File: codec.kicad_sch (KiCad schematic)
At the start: 24 parts, among them U1 UDA1380HN_N2

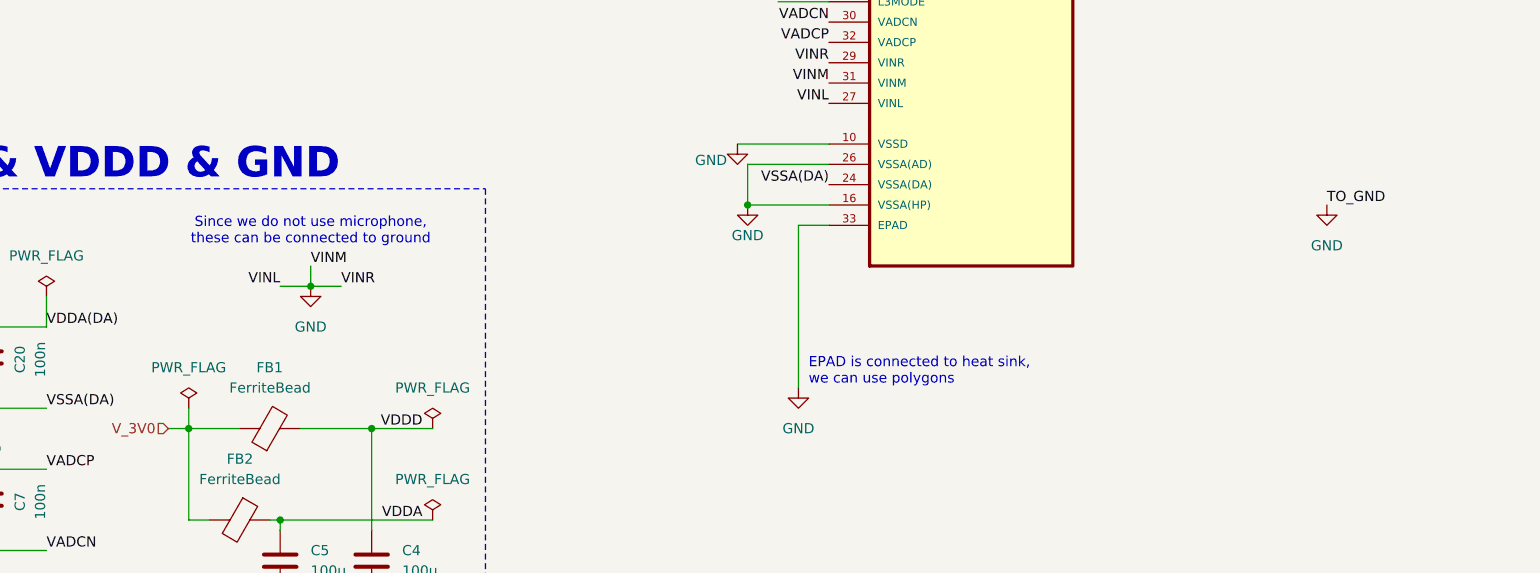
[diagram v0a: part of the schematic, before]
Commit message: Added voltage source for testing to main
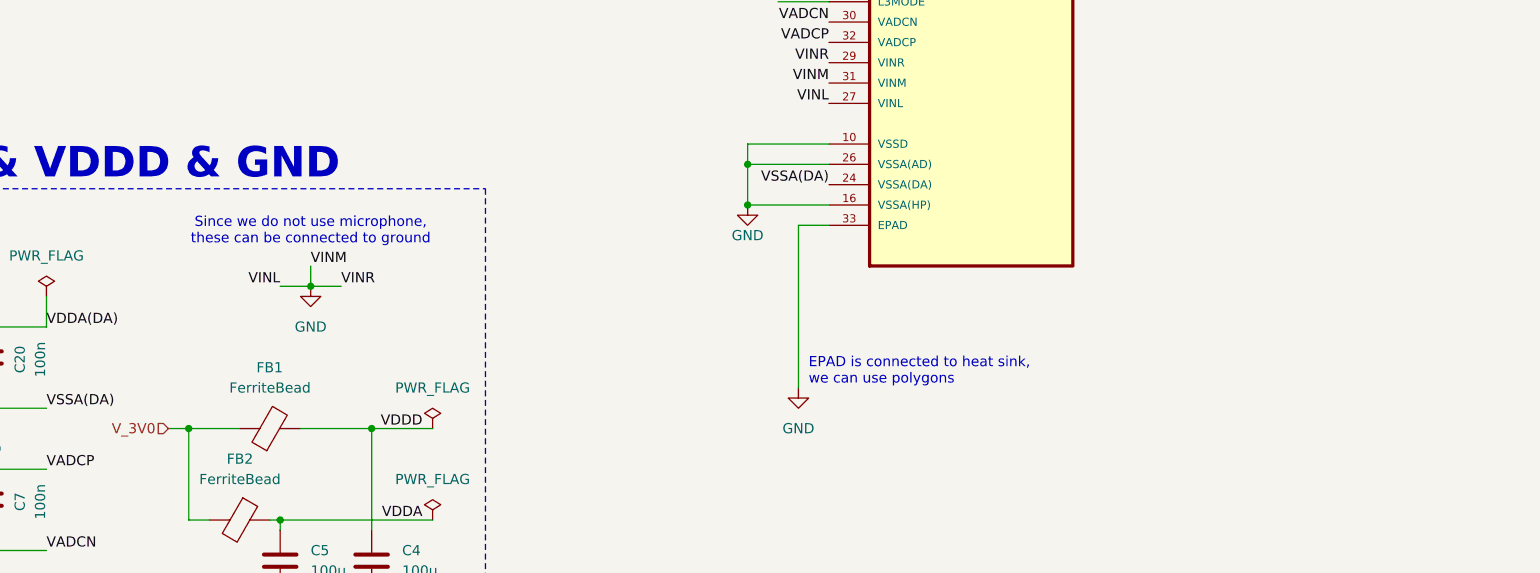
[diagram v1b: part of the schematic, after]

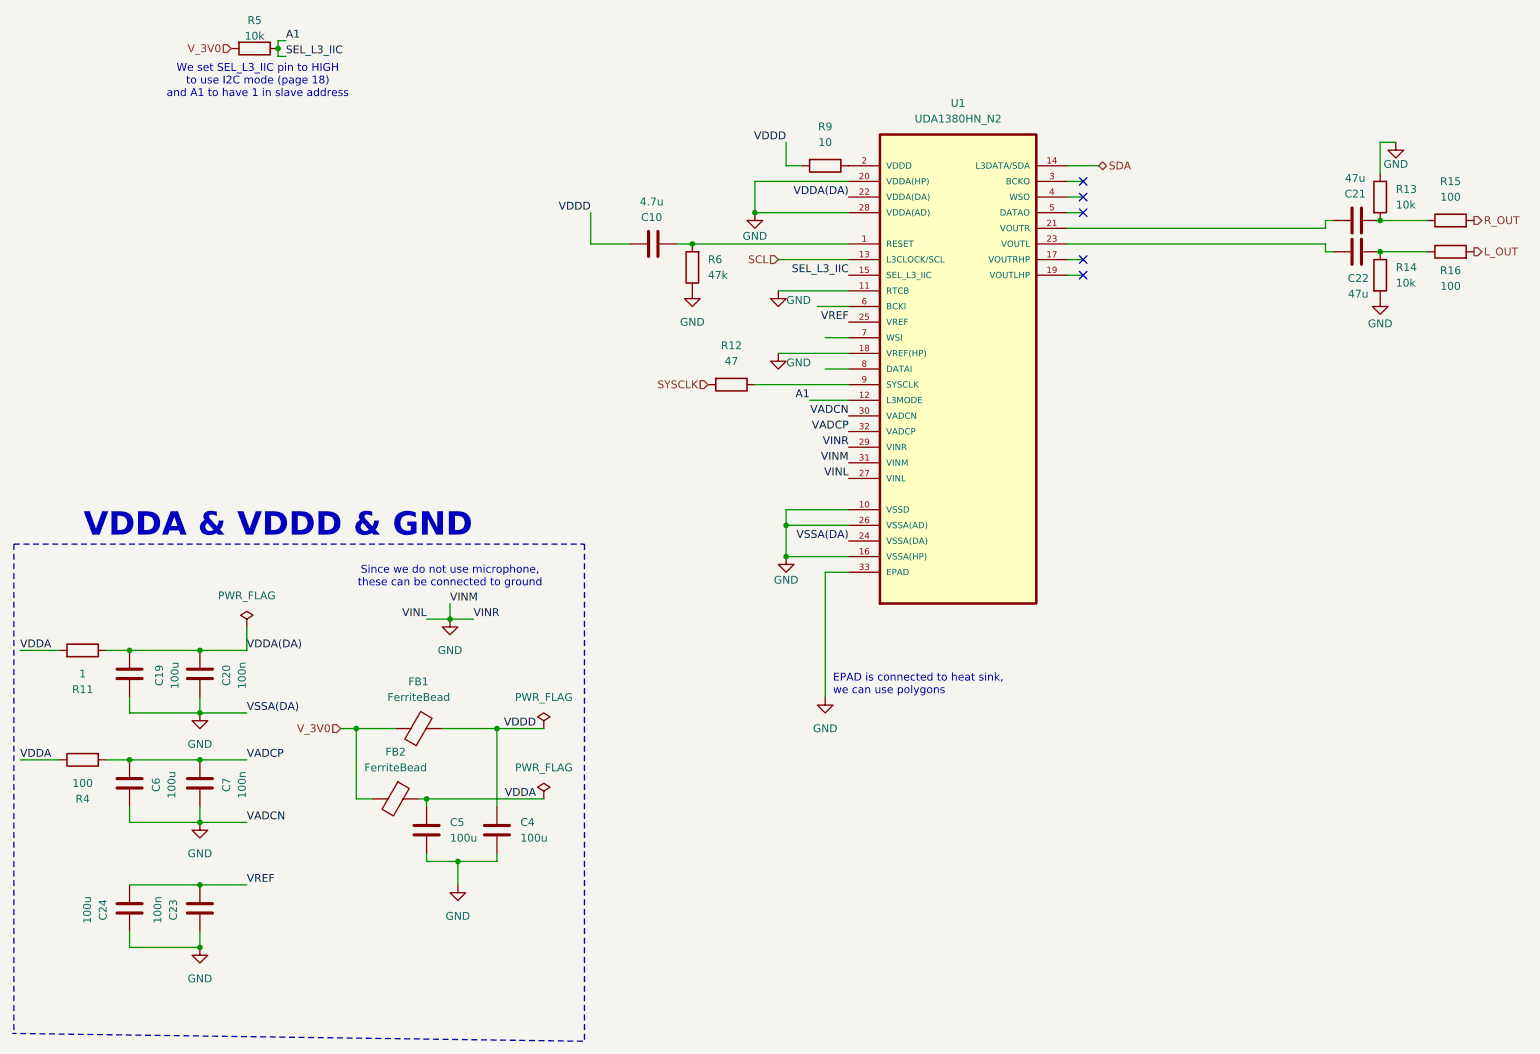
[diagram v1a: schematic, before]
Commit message: Codec finished and added notes
Corrected input and ouput pins, added NOTES file and cleaned up
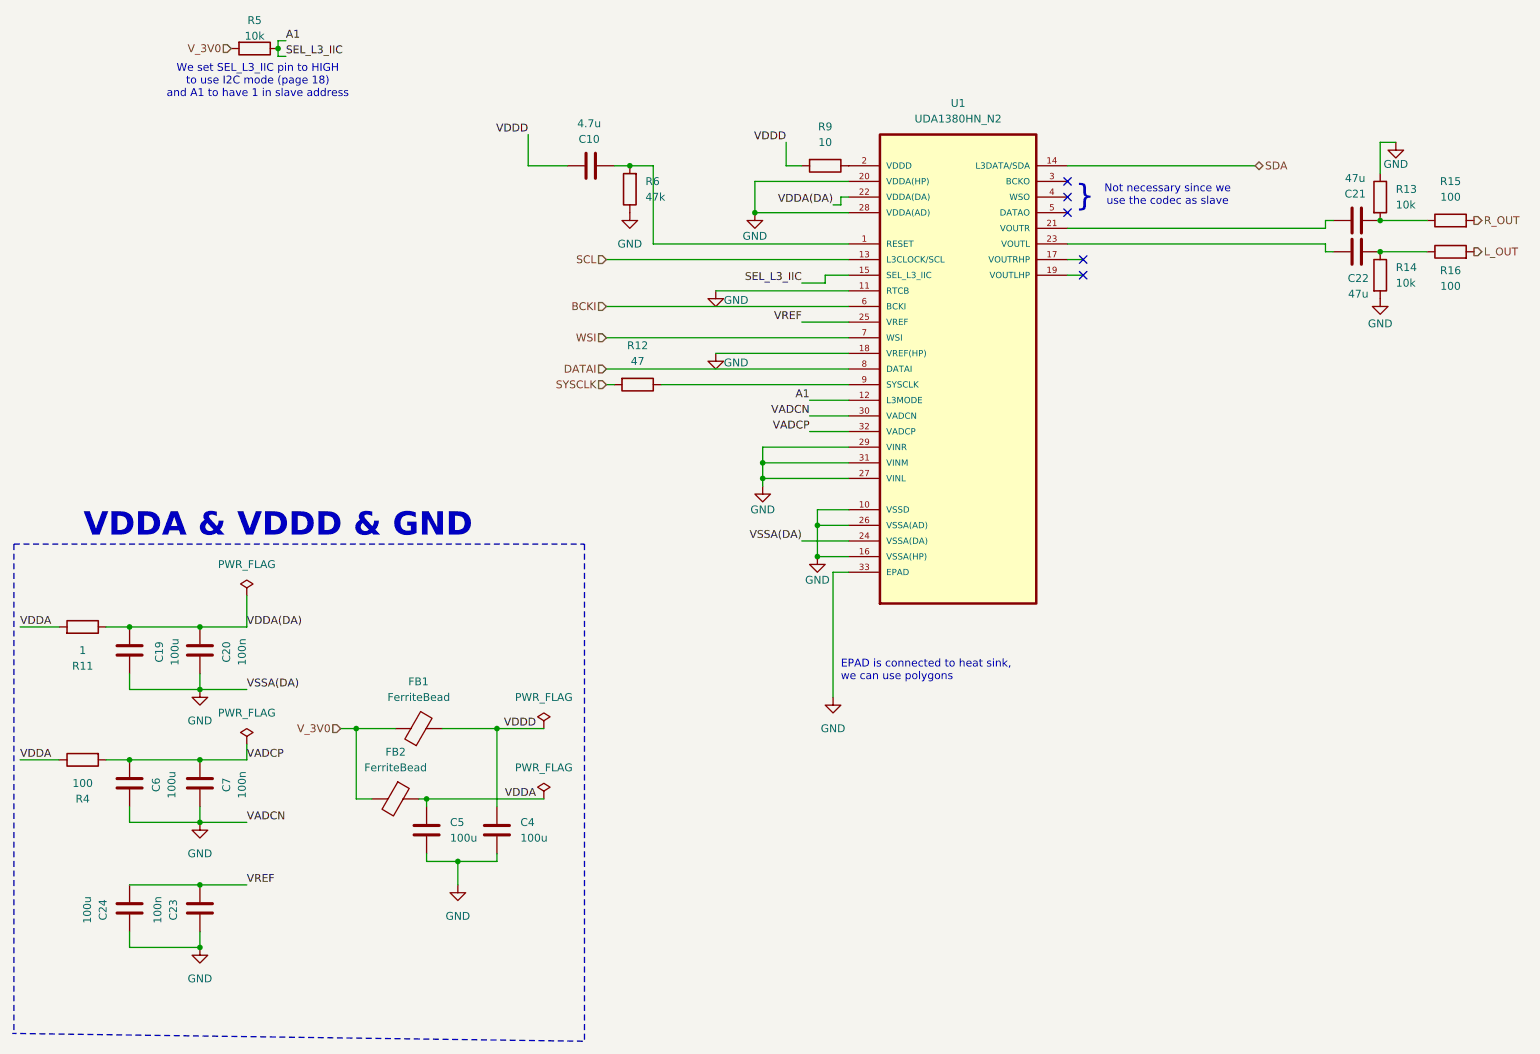
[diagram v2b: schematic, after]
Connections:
- net BCKI: now reaches U1.6 (BCKI)
- net WSI: now reaches U1.7 (WSI)
- net DATAI: now reaches U1.8 (DATAI)
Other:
- note added: "Not necessary since we use the codec as slave"
- note added: "}"
- note removed: "Since we do not use microphone, these can be connected to ground"
- moved on the sheet: C10, C19, C20, R11, R12, R6

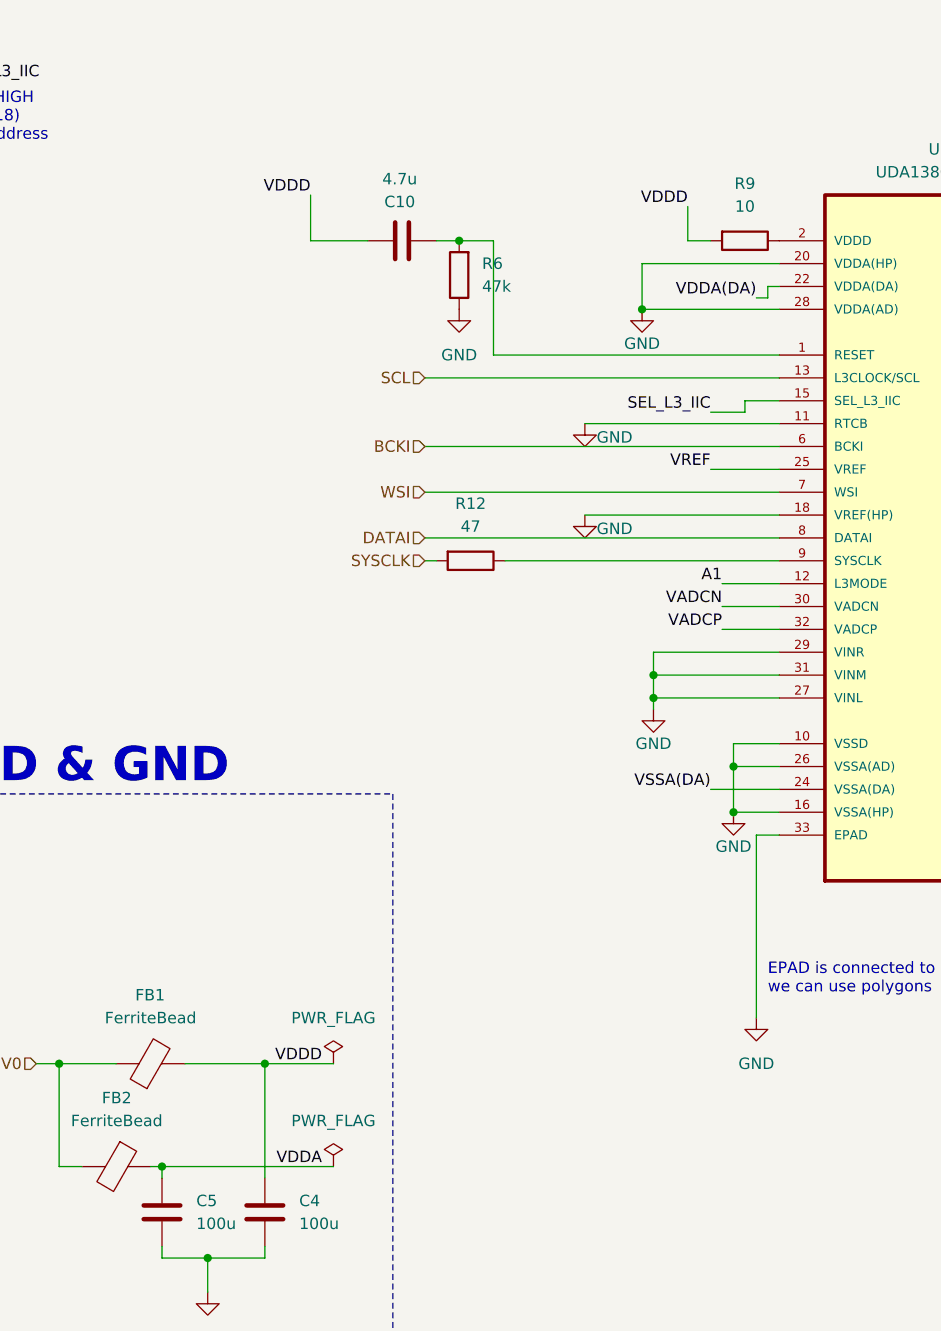
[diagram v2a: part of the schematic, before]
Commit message: Added Kitronik and cleaned connections
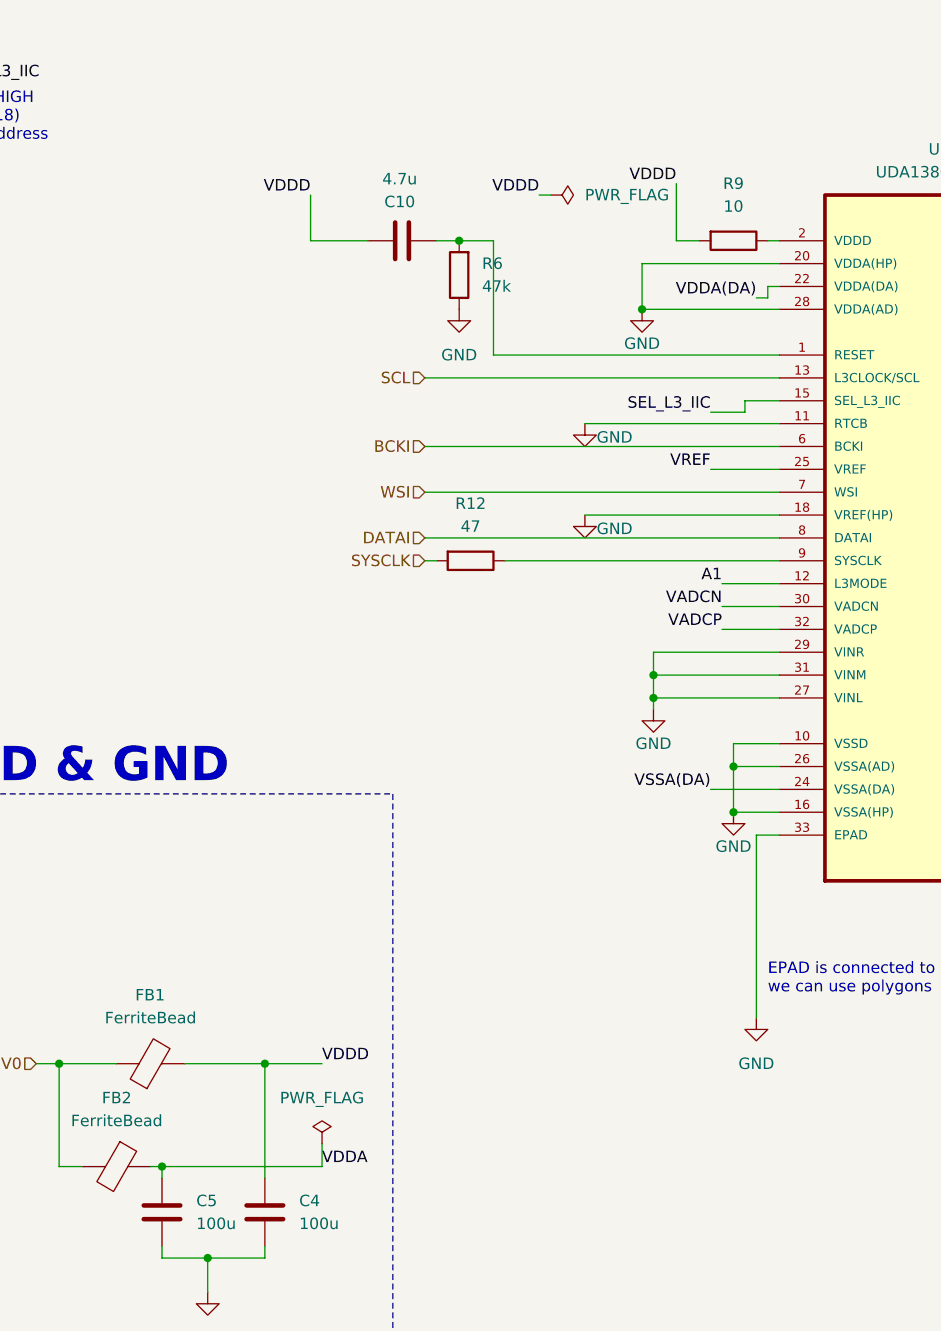
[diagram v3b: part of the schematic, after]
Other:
- moved on the sheet: R9
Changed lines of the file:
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@@
 	(wire
 		(pts
+			(xy 100.33 154.94) (xy 100.33 157.48)
+		)
+		(stroke
+			(width 0)
+			(type default)
+		)
+	)
+	(wire
+		(pts
 			(xy 53.34 129.54) (xy 45.72 129.54)
 		)
@@
 	(wire
 		(pts
-			(xy 82.55 157.48) (xy 101.6 157.48)
+			(xy 149.86 54.61) (xy 151.13 54.61)
 		)
 		(stroke
@@
 	(wire
 		(pts
-			(xy 137.16 100.33) (xy 137.16 102.87)
+			(xy 82.55 157.48) (xy 100.33 157.48)
 		)
 		(stroke
@@
 	(wire
 		(pts
-			(xy 137.16 105.41) (xy 137.16 106.68)
+			(xy 137.16 100.33) (xy 137.16 102.87)
 		)
 		(stroke
@@
 	(wire
 		(pts
-			(xy 82.55 166.37) (xy 82.55 167.64)
+			(xy 137.16 105.41) (xy 137.16 106.68)
 		)
 		(stroke
@@
 	(wire
 		(pts
-			(xy 111.76 77.47) (xy 151.13 77.47)
+			(xy 82.55 166.37) (xy 82.55 167.64)
 		)
 		(stroke
@@
 	(wire
 		(pts
-			(xy 140.97 50.8) (xy 140.97 54.61)
+			(xy 111.76 77.47) (xy 151.13 77.47)
 		)
 		(stroke
@@
 	(wire
 		(pts
-			(xy 93.98 146.05) (xy 101.6 146.05)
+			(xy 124.46 49.53) (xy 125.73 49.53)
+		)
+		(stroke
+			(width 0)
+			(type default)
+		)
+	)
+	(wire
+		(pts
+			(xy 93.98 146.05) (xy 100.33 146.05)
 		)
 		(stroke
@@
 	(wire
 		(pts
-			(xy 140.97 54.61) (xy 143.51 54.61)
+			(xy 139.7 54.61) (xy 142.24 54.61)
 		)
 		(stroke
@@
 	(wire
 		(pts
+			(xy 139.7 48.26) (xy 139.7 54.61)
+		)
+		(stroke
+			(width 0)
+			(type default)
+		)
+	)
+	(wire
+		(pts
 			(xy 45.72 171.45) (xy 34.29 171.45)
 		)
@@
 	)
 	(label "VDDD"
-		(at 100.33 146.05 180)
+		(at 139.7 48.26 180)
 		(fields_autoplaced yes)
 		(effects
@@
 		)
 	)
-	(label "VDDA"
-		(at 100.33 157.48 180)
+	(label "VDDA(DA)"
+		(at 148.59 60.96 180)
 		(fields_autoplaced yes)
 		(effects
@@
 		)
 	)
-	(label "VDDA(DA)"
-		(at 148.59 60.96 180)
+	(label "SEL_L3_IIC"
+		(at 59.69 36.83 0)
 		(fields_autoplaced yes)
 		(effects
@@
 				(size 1.27 1.27)
 			)
-			(justify right bottom)
+			(justify left bottom)
 		)
 	)
-	(label "SEL_L3_IIC"
-		(at 59.69 36.83 0)
+	(label "VDDD"
+		(at 124.46 49.53 180)
 		(fields_autoplaced yes)
 		(effects
@@
 				(size 1.27 1.27)
 			)
-			(justify left bottom)
+			(justify right bottom)
 		)
 	)
@@
 		)
 	)
-	(label "VDDD"
-		(at 140.97 50.8 180)
+	(label "A1"
+		(at 144.78 92.71 180)
 		(fields_autoplaced yes)
 		(effects
@@
 		)
 	)
-	(label "A1"
-		(at 144.78 92.71 180)
+	(label "VADCN"
+		(at 53.34 161.29 0)
 		(fields_autoplaced yes)
 		(effects
@@
 				(size 1.27 1.27)
 			)
-			(justify right bottom)
+			(justify left bottom)
 		)
 	)
-	(label "VADCN"
-		(at 53.34 161.29 0)
+	(label "VDDD"
+		(at 100.33 146.05 0)
 		(fields_autoplaced yes)
 		(effects
@@
 		)
 	)
+	(label "VDDA"
+		(at 100.33 157.48 0)
+		(fields_autoplaced yes)
+		(effects
+			(font
+				(size 1.27 1.27)
+			)
+			(justify left bottom)
+		)
+	)
 	(hierarchical_label "SCL"
 		(shape input)
@@
 	(symbol
 		(lib_id "Device:R")
-		(at 147.32 54.61 270)
+		(at 146.05 54.61 270)
 		(unit 1)
 		(exclude_from_sim no)
@@
 		(fields_autoplaced yes)
 		(property "Reference" "R9"
-			(at 147.32 48.26 90)
+			(at 146.05 48.26 90)
 			(effects
 				(font
@@
 		)
 		(property "Value" "10"
-			(at 147.32 50.8 90)
+			(at 146.05 50.8 90)
 			(effects
 				(font
@@
 		)
 		(property "Footprint" ""
-			(at 147.32 52.832 90)
+			(at 146.05 52.832 90)
 			(effects
 				(font
@@
 		)
 		(property "Datasheet" "~"
-			(at 147.32 54.61 0)
+			(at 146.05 54.61 0)
 			(effects
 				(font
@@
 		)
 		(property "Description" "Resistor"
-			(at 147.32 54.61 0)
+			(at 146.05 54.61 0)
 			(effects
 				(font
@@
 	(symbol
 		(lib_id "power:PWR_FLAG")
+		(at 125.73 49.53 270)
+		(unit 1)
+		(exclude_from_sim no)
+		(in_bom yes)
+		(on_board yes)
+		(dnp no)
+		(fields_autoplaced yes)
+		(property "Reference" "#FLG05"
+			(at 127.635 49.53 0)
+			(effects
+				(font
+					(size 1.27 1.27)
+				)
+				(hide yes)
+			)
+		)
+		(property "Value" "PWR_FLAG"
+			(at 129.54 49.5299 90)
+			(effects
+				(font
+					(size 1.27 1.27)
+				)
+				(justify left)
+			)
+		)
+		(property "Footprint" ""
+			(at 125.73 49.53 0)
+			(effects
+				(font
+					(size 1.27 1.27)
+				)
+				(hide yes)
+			)
+		)
+		(property "Datasheet" "~"
+			(at 125.73 49.53 0)
+			(effects
+				(font
+					(size 1.27 1.27)
+				)
+				(hide yes)
+			)
+		)
+		(property "Description" "Special symbol for telling ERC where power comes from"
+			(at 125.73 49.53 0)
+			(effects
+				(font
+					(size 1.27 1.27)
+				)
+				(hide yes)
+			)
+		)
+		(pin "1"
+		)
+		(instances
+			(project "plant caretaker"
+				(path "/23b35dcc-615e-4aec-abee-c26cc3d8b906/34ae70cd-ec6d-4009-8d65-9818ae1eafe0"
+					(reference "#FLG05")
+					(unit 1)
+				)
+			)
+		)
+	)
+	(symbol
+		(lib_id "power:PWR_FLAG")
 		(at 53.34 124.46 0)
 		(unit 1)
@@
 	(symbol
 		(lib_id "power:PWR_FLAG")
-		(at 101.6 157.48 0)
+		(at 100.33 154.94 0)
 		(unit 1)
 		(exclude_from_sim no)
@@
 		(dnp no)
 		(fields_autoplaced yes)
-		(property "Reference" "#FLG07"
-			(at 101.6 155.575 0)
+		(property "Reference" "#FLG06"
+			(at 100.33 153.035 0)
 			(effects
 				(font
@@
 		)
 		(property "Value" "PWR_FLAG"
-			(at 101.6 152.4 0)
+			(at 100.33 149.86 0)
 			(effects
 				(font
@@
 		)
 		(property "Footprint" ""
-			(at 101.6 157.48 0)
+			(at 100.33 154.94 0)
 			(effects
 				(font
@@
 		)
 		(property "Datasheet" "~"
-			(at 101.6 157.48 0)
+			(at 100.33 154.94 0)
 			(effects
 				(font
@@
 		)
 		(property "Description" "Special symbol for telling ERC where power comes from"
-			(at 101.6 157.48 0)
+			(at 100.33 154.94 0)
 			(effects
 				(font
@@
 			(project "plant caretaker"
 				(path "/23b35dcc-615e-4aec-abee-c26cc3d8b906/34ae70cd-ec6d-4009-8d65-9818ae1eafe0"
-					(reference "#FLG07")
+					(reference "#FLG06")
 					(unit 1)
 				)
@@
 					(unit 1)
 				)
-			)
-		)
-	)
-	(symbol
-		(lib_id "power:PWR_FLAG")
-		(at 101.6 146.05 0)
-		(unit 1)
-		(exclude_from_sim no)
-		(in_bom yes)
-		(on_board yes)
-		(dnp no)
-		(fields_autoplaced yes)
-		(property "Reference" "#FLG06"
-			(at 101.6 144.145 0)
-			(effects
-				(font
-					(size 1.27 1.27)
-				)
-				(hide yes)
-			)
-		)
-		(property "Value" "PWR_FLAG"
-			(at 101.6 140.97 0)
-			(effects
-				(font
-					(size 1.27 1.27)
-				)
-			)
-		)
-		(property "Footprint" ""
-			(at 101.6 146.05 0)
-			(effects
-				(font
-					(size 1.27 1.27)
-				)
-				(hide yes)
-			)
-		)
-		(property "Datasheet" "~"
-			(at 101.6 146.05 0)
-			(effects
-				(font
-					(size 1.27 1.27)
-				)
-				(hide yes)
-			)
-		)
-		(property "Description" "Special symbol for telling ERC where power comes from"
-			(at 101.6 146.05 0)
-			(effects
-				(font
-					(size 1.27 1.27)
-				)
-				(hide yes)
-			)
-		)
-		(pin "1"
-		)
-		(instances
-			(project "plant caretaker"
-				(path "/23b35dcc-615e-4aec-abee-c26cc3d8b906/34ae70cd-ec6d-4009-8d65-9818ae1eafe0"
-					(reference "#FLG06")
-					(unit 1)
-				)
